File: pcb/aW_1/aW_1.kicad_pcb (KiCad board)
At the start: 2 copper layers, 145.1 x 114.9 mm, 113 parts, among them J1 USB4110-GF-A, J2 USB4110-GF-A, J3 USB4110-GF-A, J4 Conn_ARM_JTAG_SWD_10, K1 KEYSW, K10 KEYSW, K11 KEYSW, K12 KEYSW, K13 KEYSW, K14 KEYSW, K15 KEYSW, K16 KEYSW, K17 KEYSW, K18 KEYSW, K19 KEYSW, K2 KEYSW, K20 KEYSW, K21 KEYSW, K22 KEYSW, K23 KEYSW, K24 KEYSW, K25 KEYSW, K26 KEYSW, K27 KEYSW, K28 KEYSW, K29 KEYSW, K3 KEYSW, K30 KEYSW, K31 KEYSW, K32 KEYSW, K33 KEYSW, K4 KEYSW, K5 KEYSW, K6 KEYSW, K7 KEYSW, K8 KEYSW, K9 KEYSW, Q1 Q_PMOS_SDG, SW1 BTN1, SW2 BTN2, U1 AP2112K-3.3TRG1, U2 MCP23017T-E_SS, U3 MCP73831-2-OT, U4 FT231XS-R, U5 BL652-SA-01-T_R, Y1 32.768

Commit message: Added voltage divider for battery measurement, improved gnd pour
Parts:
- added R16: 806K, Resistor_SMD:R_0603_1608Metric, F.Cu at (170.5, 48.0)
- added R17: 2M, Resistor_SMD:R_0603_1608Metric, F.Cu at (172.3, 48.0)
- moved C4 1.18 mm to (164.6, 48.0)
- moved C5 1.18 mm to (168.2, 48.0)
- moved R2 1.18 mm to (163.4, 48.0)
- moved R7 1.18 mm to (167.0, 48.0)
- moved R6 1.18 mm to (165.8, 48.0)
- moved U3 1.18 mm to (166.4, 44.4)
- moved C13 0.79 mm to (85.3, 50.3)
- moved C12 0.59 mm to (79.3, 50.3)
- moved Y1 0.59 mm to (82.3, 50.3)
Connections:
- U5 pad 21: /btn2 -> /bsense
- U5 pad 22: Net-(U5-Pad22) -> /btn2
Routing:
- net /bsense: track 0.00 -> 90.8 mm
- net VDC: track 145.3 -> 183.0 mm
- net GND: track 98.0 -> 122.5 mm, vias 27 -> 40
- net VBUS: track 103.3 -> 100.6 mm
- net Net-(D2-Pad1): track 56.4 -> 58.4 mm
- net Net-(C12-Pad1): track 5.05 -> 6.22 mm
- net /col5: track 449.0 -> 448.0 mm
- net /col2: track 307.5 -> 306.4 mm
- net /col3: track 346.5 -> 345.5 mm
- net /col0: track 483.2 -> 482.2 mm
- net /btn2: track 48.0 -> 48.7 mm

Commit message: Cleaned up layout, updated gerbers
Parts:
- moved R17 20.1 mm to (152.2, 47.4), turned to 270 degrees
- moved C2 19.0 mm to (132.6, 47.4)
- moved C3 19.0 mm to (136.8, 47.4)
- moved C4 19.0 mm to (145.7, 47.4)
- moved C5 19.0 mm to (149.2, 47.4)
- moved D1 19.0 mm to (140.3, 47.4)
- moved Q1 19.0 mm to (140.3, 43.8)
- moved R2 19.0 mm to (144.5, 47.4)
- moved R3 19.0 mm to (134.4, 47.4)
- moved R6 19.0 mm to (146.9, 47.4)
- moved U1 19.0 mm to (134.4, 43.7)
- moved U3 19.0 mm to (147.4, 43.8)
- moved R7 19.0 mm to (148.0, 47.4)
- moved R16 18.8 mm to (152.2, 43.8)
- moved R4 4.27 mm to (149.8, 34.9), turned to 270 degrees
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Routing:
- net VDC: track 183.0 -> 144.5 mm
- net Net-(C2-Pad1): track 35.9 -> 57.5 mm
- net Net-(D2-Pad1): track 58.4 -> 41.2 mm
- net /bsense: track 90.8 -> 73.9 mm
- net VBUS: track 100.6 -> 86.1 mm
- net +BATT: track 59.1 -> 73.1 mm
- net GND: track 122.5 -> 110.7 mm
- net +3V3: track 209.6 -> 213.0 mm, vias 8 -> 7
- net Net-(J3-PadA5): track 5.99 -> 8.40 mm
- net Net-(J3-PadB5): track 6.02 -> 7.93 mm
- net /reset: track 50.2 -> 51.7 mm
- net /sda_left: track 117.5 -> 118.2 mm
- net /btn2: track 48.7 -> 49.3 mm
- net /main_usb_dp: track 32.1 -> 31.5 mm
- net /main_usb_dn: track 31.9 -> 31.3 mm
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
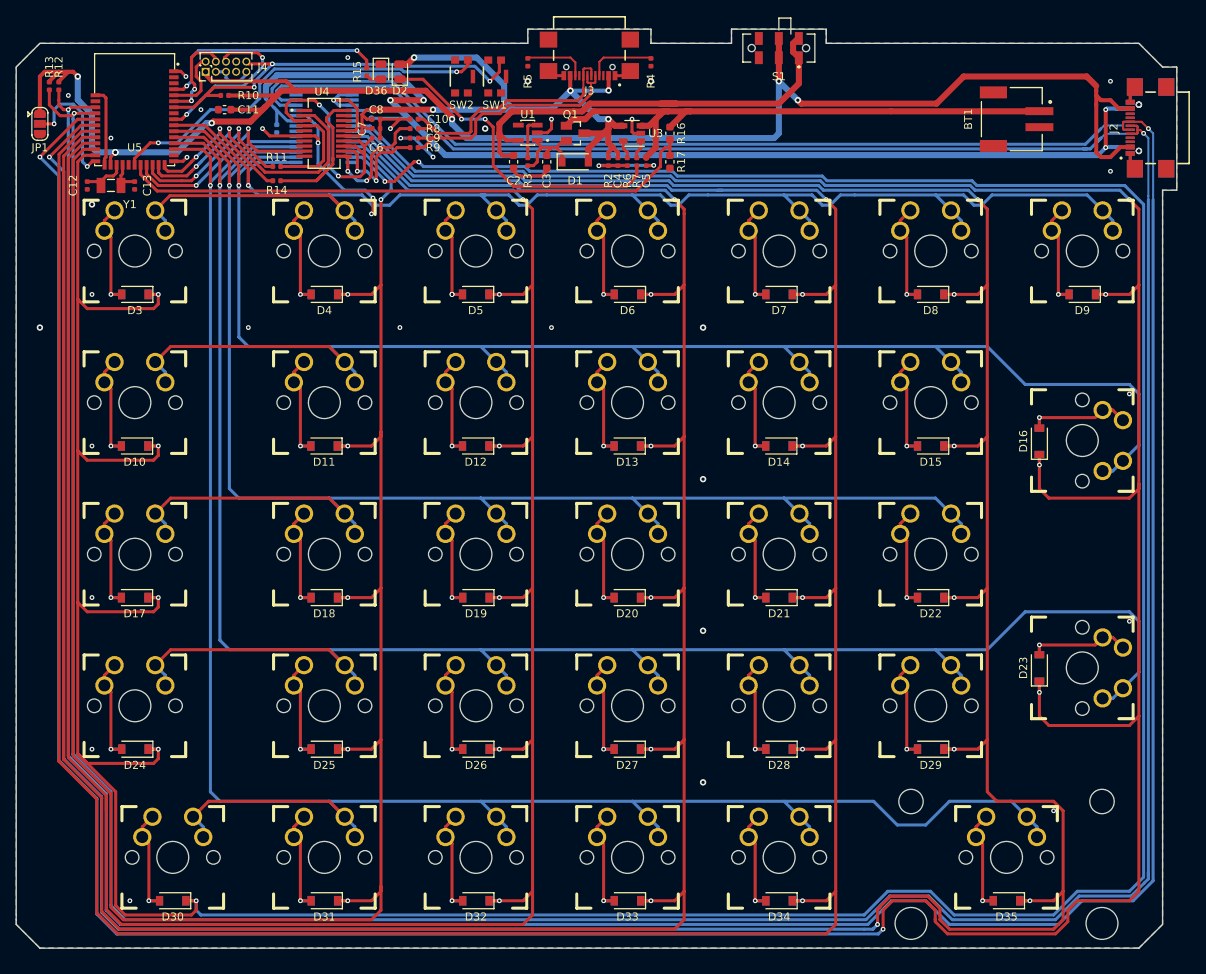
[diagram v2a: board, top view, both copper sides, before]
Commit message: Modified traces around spacebar stab mounts for additional clearance
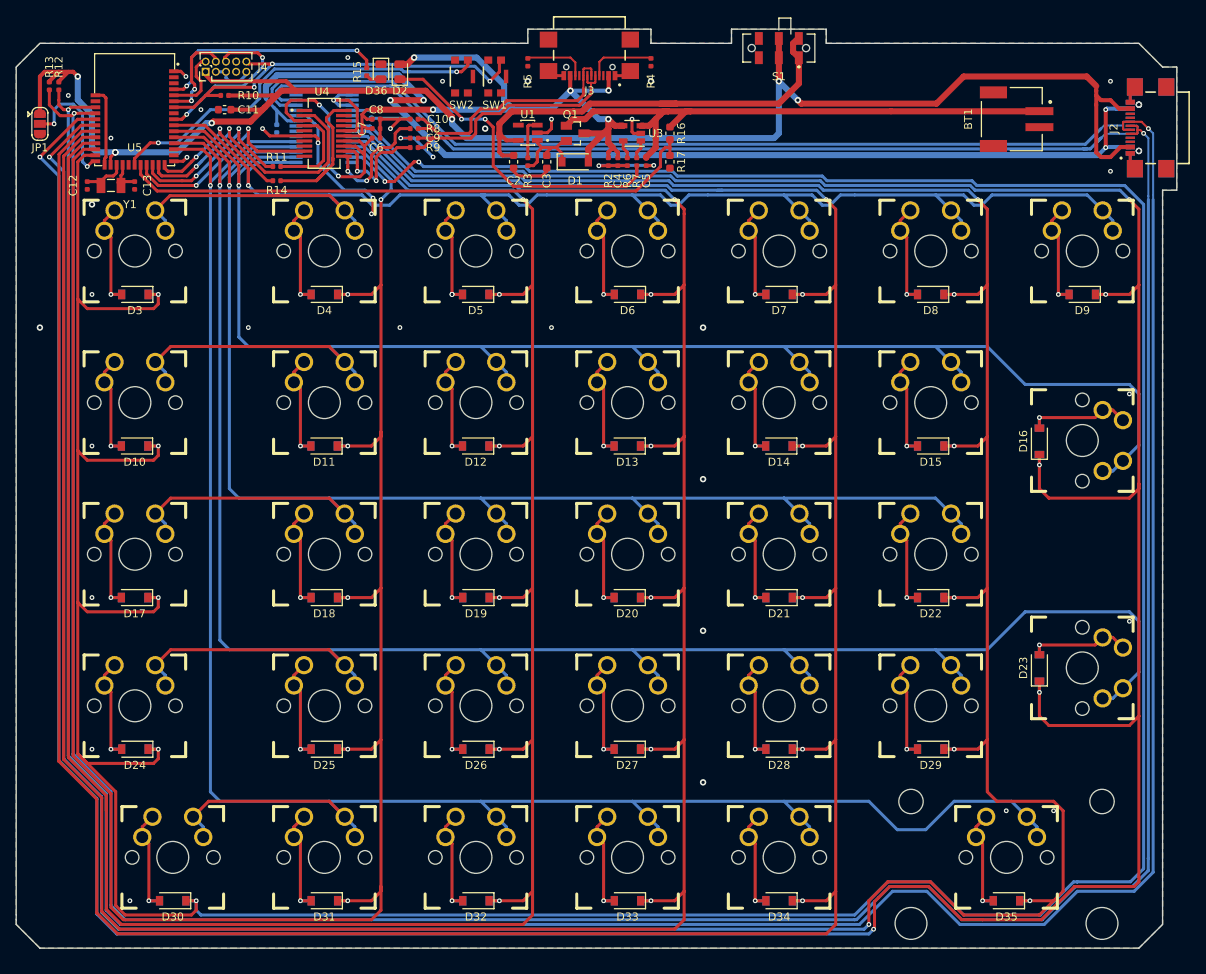
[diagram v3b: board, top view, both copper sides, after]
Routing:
- net /col5: track 448.0 -> 443.8 mm
- net /col6: track 480.5 -> 478.8 mm
- net GND: vias 40 -> 42

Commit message: Fixed mosfet and improved keepout around antenna
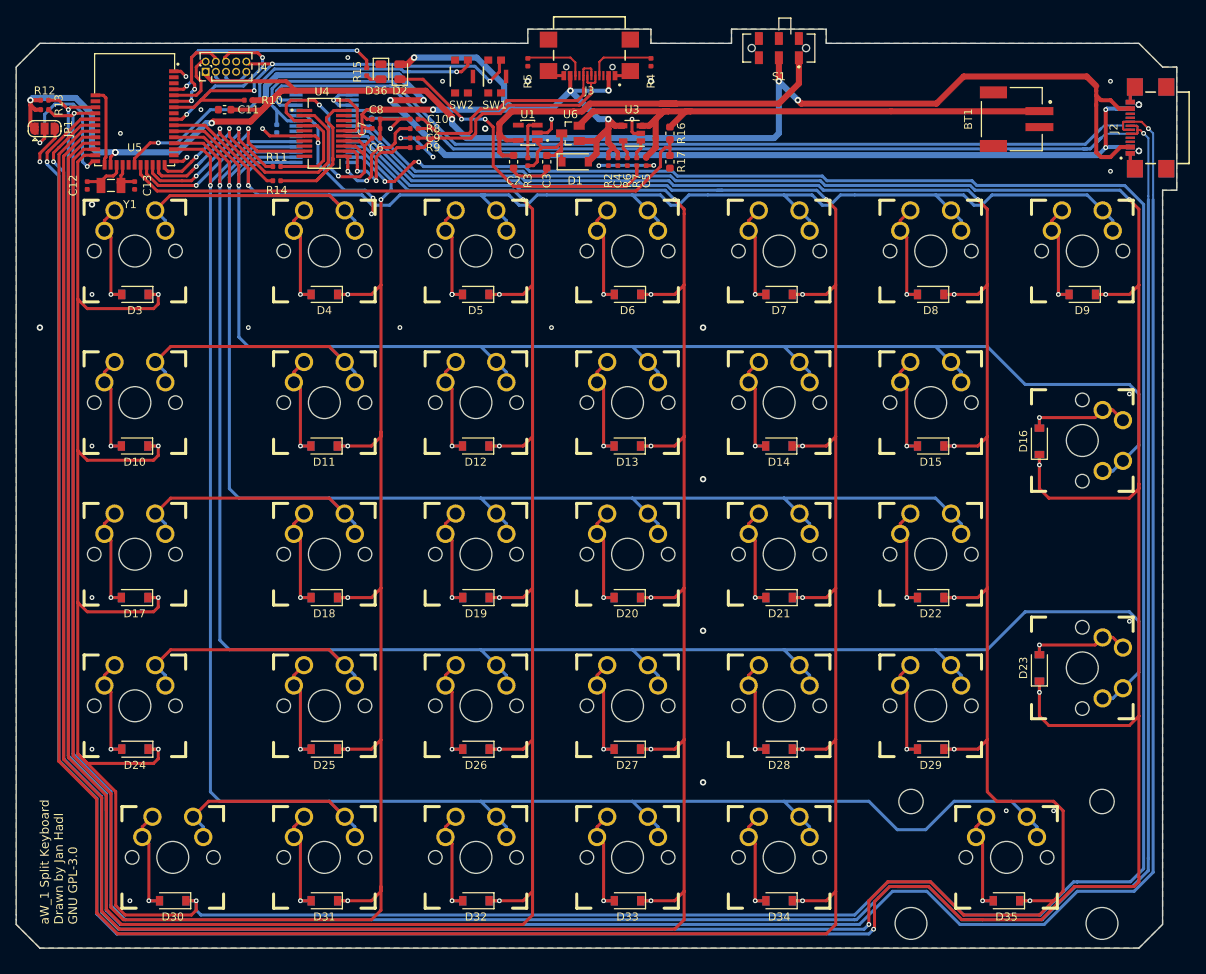
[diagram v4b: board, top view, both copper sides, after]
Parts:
- removed Q1: Q_PMOS_SDG, snap-eda:SOT23
- added U6: DMP2035U-7, snap-eda:SOT23, F.Cu at (139.7, 43.8)
- moved R10 3.02 mm to (99.5, 39.7)
- moved R13 3.02 mm to (74.0, 40.9), turned to 180 degrees
- moved R12 2.51 mm to (74.0, 39.7), turned to 180 degrees
- moved JP1 0.84 mm to (74.0, 43.2), turned to 0 degrees
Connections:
- S1 pad 4: Net-(C2-Pad1) -> Net-(S1-Pad4)
- S1 pad 5: +3V3 -> Net-(S1-Pad5)
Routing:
- net +3V3: track 213.0 -> 205.2 mm
- net /reset: track 51.7 -> 55.4 mm
- net Net-(JP1-Pad2): track 16.0 -> 19.7 mm
- net Net-(C2-Pad1): track 57.5 -> 54.4 mm
- net GND: track 110.7 -> 113.4 mm
- net /scl_right: track 341.8 -> 339.8 mm
- net +BATT: track 73.1 -> 71.6 mm
- net Net-(C3-Pad1): track 13.0 -> 13.9 mm
- net /col6: track 478.8 -> 479.4 mm
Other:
- board text added: "aW_1 Split Keyboard Drawn by Jan Hadl GNU GPL-3.0"

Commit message: Added 1mm of clearance to the bottom side (for spacebar mounting holes)
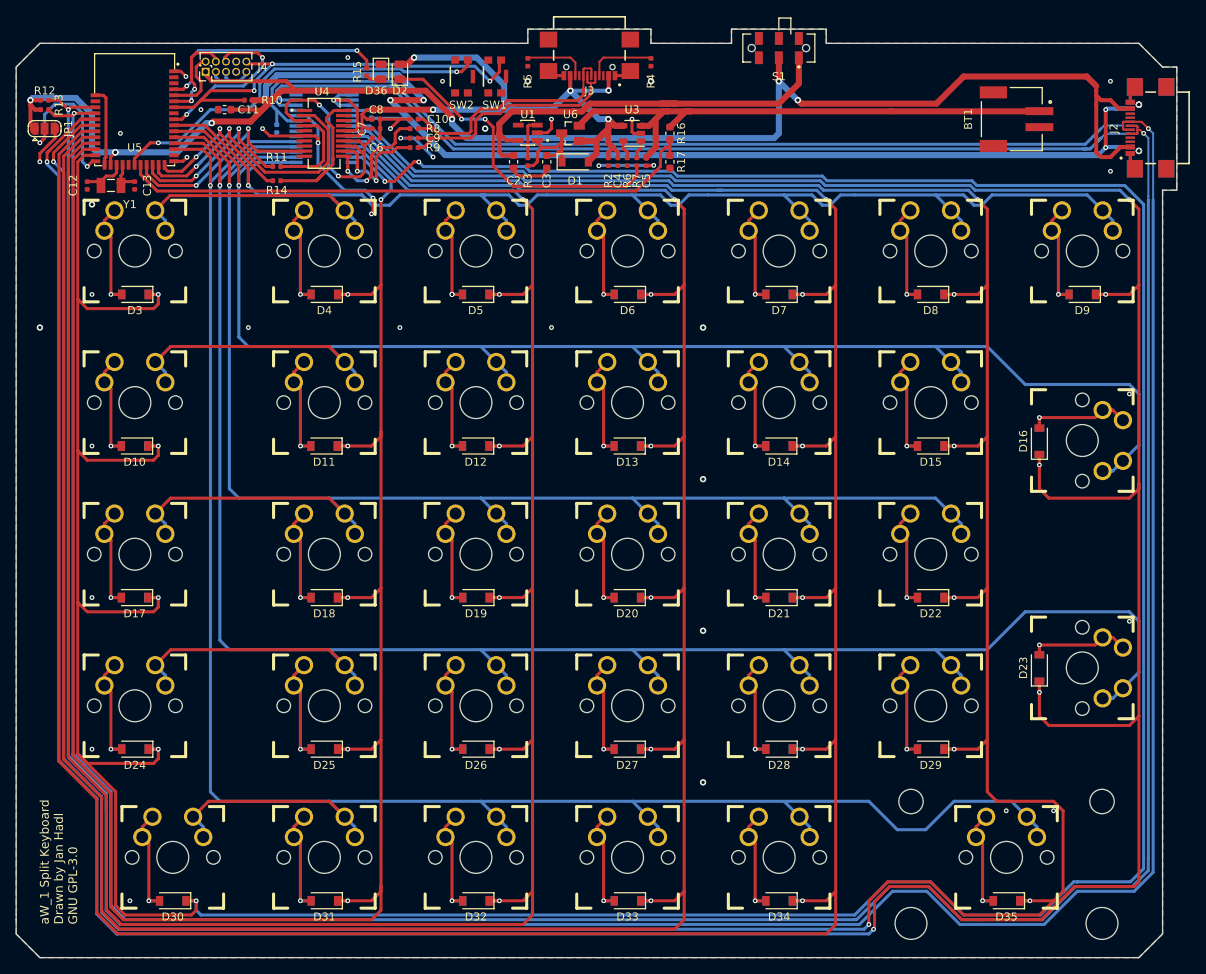
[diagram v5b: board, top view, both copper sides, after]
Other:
- board size 145.1 x 114.9 mm -> 145.1 x 116.1 mm
